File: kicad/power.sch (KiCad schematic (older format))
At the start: 42 parts, among them Q1 BC857, Q2 BC847, Q3 BC857, U4 AP62201-SOT563, U5 AP62201-SOT563, U6 TLV71x, U7 TLV71x

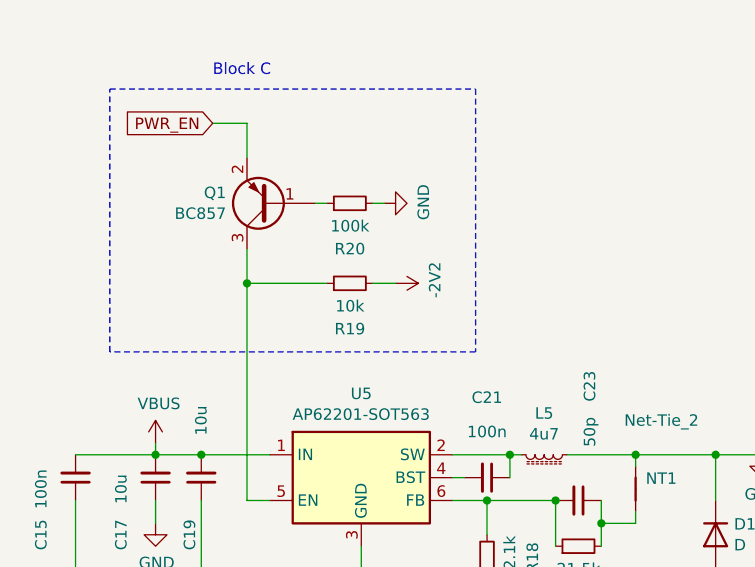
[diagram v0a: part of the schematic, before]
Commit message: removed frontent/amp test circuit
This circuit had shared the PCB for cost reasons.
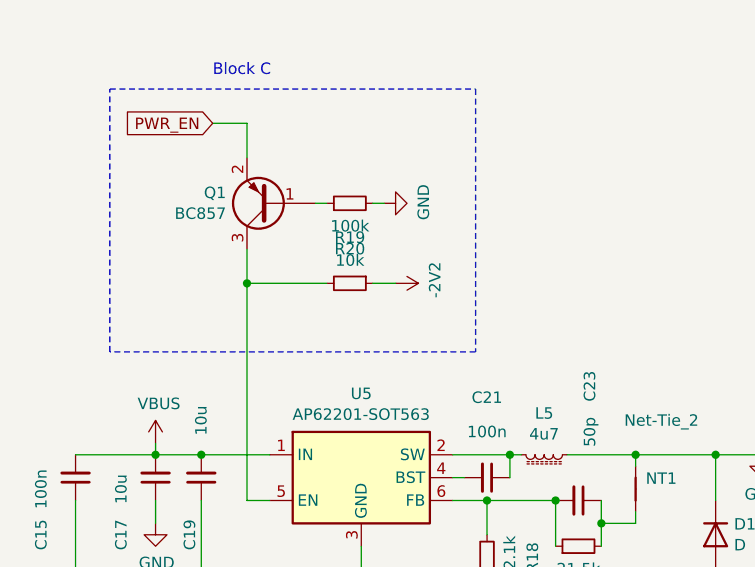
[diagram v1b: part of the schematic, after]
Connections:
- net -2V2: now also R19.1; no longer R19.2
- net at Q1.3 (C), U5.5 (EN): now also R19.2; no longer R19.1
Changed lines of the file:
@@
 $Descr A4 11693 8268
 encoding utf-8
-Sheet 4 5
+Sheet 4 4
 Title ""
 Date ""
@@
 F 3 "~" H 2900 4800 50  0001 C CNN
 	1    2900 4800
-	0    -1   -1   0
+	0    1    1    0
 $EndComp
 $Comp
@@
 AR Path="/6273F58A" Ref="#PWR?"  Part="1"
 AR Path="/624595FA/6273F58A" Ref="#PWR?"  Part="1"
-AR Path="/623B3927/6273F58A" Ref="#PWR?"  Part="1"
-F 0 "#PWR?" H 3100 4650 50  0001 C CNN
+AR Path="/623B3927/6273F58A" Ref="#PWR0105"  Part="1"
+F 0 "#PWR0105" H 3100 4650 50  0001 C CNN
 F 1 "-2V2" H 3115 4973 50  0000 C CNN
 F 2 "" H 3100 4800 50  0001 C CNN
